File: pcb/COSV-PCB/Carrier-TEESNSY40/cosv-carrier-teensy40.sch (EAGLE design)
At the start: 25 parts, among them X1 057-006-1, X3 22-23-2031, X4 22-23-2031, X5 22-23-2031, X6 22-23-2031, X7 22-23-2031

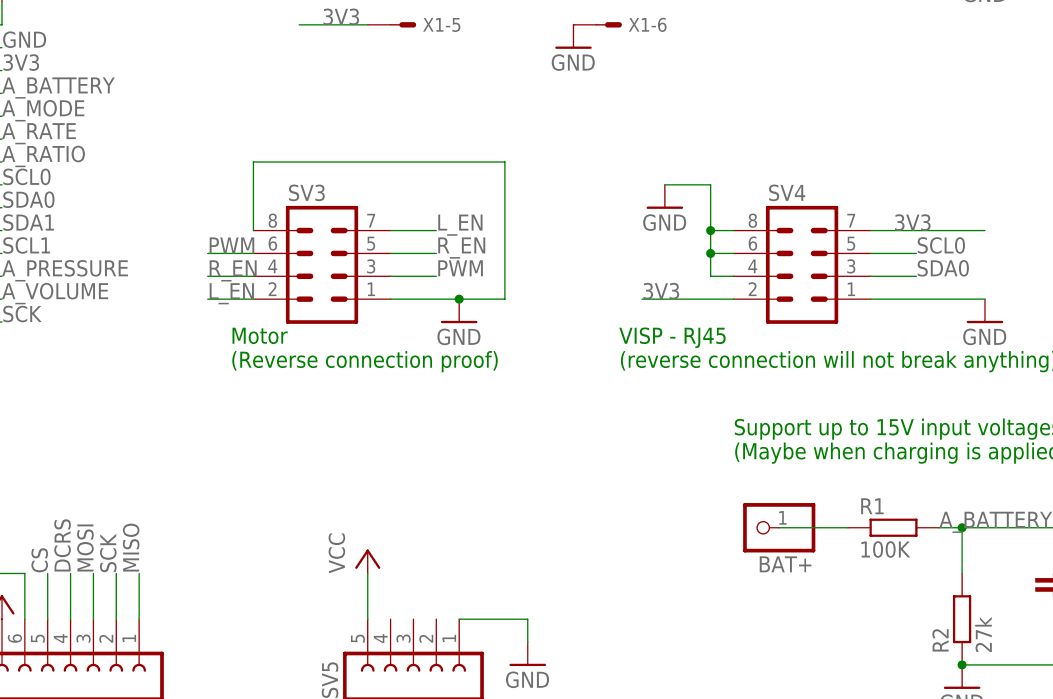
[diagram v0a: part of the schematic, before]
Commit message: Make the motor connector identical to the Arduino IBT_2 H-Bridge
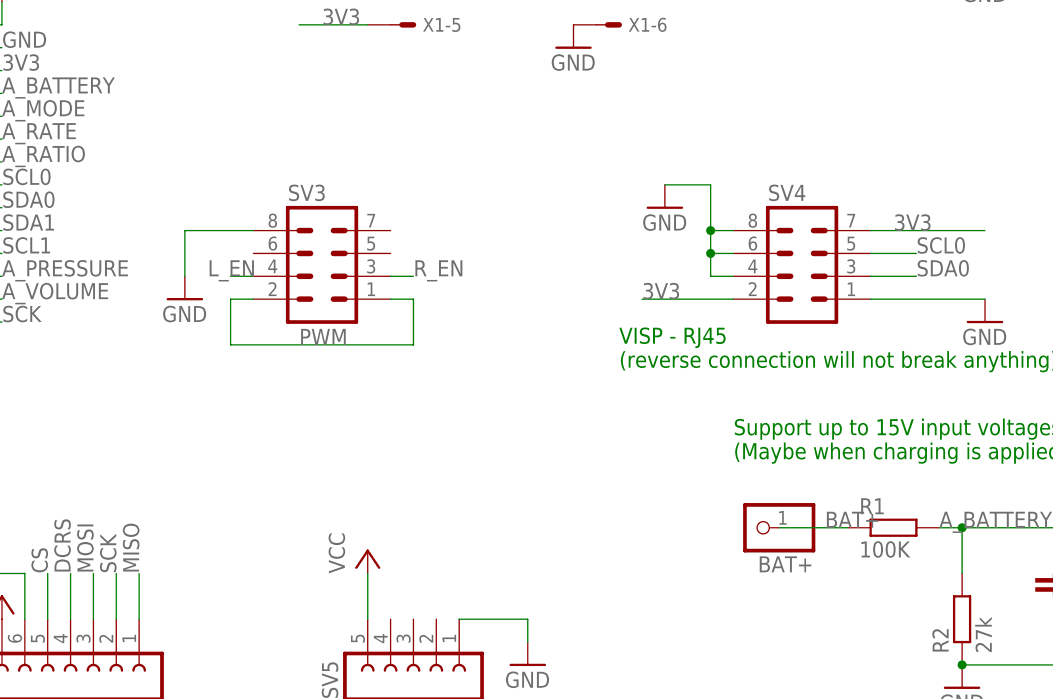
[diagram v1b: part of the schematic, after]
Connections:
- net N$2 renamed BAT+
- net GND: no longer SV3.1
- net L_EN: now also SV3.4; no longer SV3.2, SV3.7
- net PWM: now also SV3.1, SV3.2; no longer SV3.3, SV3.6
- net R_EN: now also SV3.3; no longer SV3.4, SV3.5
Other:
- note removed: "Motor (Reverse connection proof)"
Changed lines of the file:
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@@
 <?xml version="1.0" encoding="utf-8"?>
 <!DOCTYPE eagle SYSTEM "eagle.dtd">
-<eagle version="7.7.0">
+<eagle version="7.6.0">
 <drawing>
 <settings>
@@
 (Reverse connection swaps HOME/ENCODER)
 (Can be identified in software)</text>
-<text x="60.96" y="48.26" size="1.778" layer="91">Motor
-(Reverse connection proof)</text>
 <text x="104.14" y="48.26" size="1.778" layer="91">VISP - RJ45
 (reverse connection will not break anything)</text>
@@
 <instance part="GND5" gate="1" x="144.78" y="53.34"/>
 <instance part="GND9" gate="1" x="109.22" y="66.04"/>
-<instance part="GND10" gate="1" x="86.36" y="53.34"/>
+<instance part="GND10" gate="1" x="55.88" y="55.88"/>
 <instance part="GND11" gate="1" x="99.06" y="83.82"/>
 <instance part="GND12" gate="1" x="58.42" y="93.98"/>
@@
 </segment>
 <segment>
-<pinref part="SV3" gate="G$1" pin="1"/>
-<pinref part="GND10" gate="1" pin="GND"/>
-<wire x1="78.74" y1="55.88" x2="86.36" y2="55.88" width="0.1524" layer="91"/>
-<pinref part="SV3" gate="G$1" pin="8"/>
-<wire x1="63.5" y1="63.5" x2="63.5" y2="71.12" width="0.1524" layer="91"/>
-<wire x1="63.5" y1="71.12" x2="91.44" y2="71.12" width="0.1524" layer="91"/>
-<wire x1="91.44" y1="71.12" x2="91.44" y2="55.88" width="0.1524" layer="91"/>
-<wire x1="91.44" y1="55.88" x2="86.36" y2="55.88" width="0.1524" layer="91"/>
-<junction x="86.36" y="55.88"/>
-</segment>
-<segment>
 <pinref part="X1" gate="-6" pin="S"/>
 <pinref part="GND11" gate="1" pin="GND"/>
@@
 <pinref part="GND13" gate="1" pin="GND"/>
 <wire x1="27.94" y1="25.4" x2="27.94" y2="20.32" width="0.1524" layer="91"/>
+</segment>
+<segment>
+<pinref part="SV3" gate="G$1" pin="8"/>
+<pinref part="GND10" gate="1" pin="GND"/>
+<wire x1="63.5" y1="63.5" x2="55.88" y2="63.5" width="0.1524" layer="91"/>
+<wire x1="55.88" y1="63.5" x2="55.88" y2="58.42" width="0.1524" layer="91"/>
 </segment>
 </net>
@@
 </segment>
 <segment>
-<pinref part="SV3" gate="G$1" pin="5"/>
-<wire x1="78.74" y1="60.96" x2="83.82" y2="60.96" width="0.1524" layer="91"/>
-<label x="83.82" y="60.96" size="1.778" layer="95"/>
-</segment>
-<segment>
-<pinref part="SV3" gate="G$1" pin="4"/>
-<wire x1="63.5" y1="58.42" x2="58.42" y2="58.42" width="0.1524" layer="91"/>
-<label x="58.42" y="58.42" size="1.778" layer="95"/>
+<pinref part="SV3" gate="G$1" pin="3"/>
+<wire x1="78.74" y1="58.42" x2="81.28" y2="58.42" width="0.1524" layer="91"/>
+<label x="81.28" y="58.42" size="1.778" layer="95"/>
 </segment>
 </net>
@@
 </segment>
 <segment>
-<pinref part="SV3" gate="G$1" pin="7"/>
-<wire x1="78.74" y1="63.5" x2="83.82" y2="63.5" width="0.1524" layer="91"/>
-<label x="83.82" y="63.5" size="1.778" layer="95"/>
-</segment>
-<segment>
-<pinref part="SV3" gate="G$1" pin="2"/>
-<wire x1="63.5" y1="55.88" x2="58.42" y2="55.88" width="0.1524" layer="91"/>
-<label x="58.42" y="55.88" size="1.778" layer="95"/>
+<pinref part="SV3" gate="G$1" pin="4"/>
+<wire x1="63.5" y1="58.42" x2="60.96" y2="58.42" width="0.1524" layer="91"/>
+<label x="58.42" y="58.42" size="1.778" layer="95"/>
 </segment>
 </net>
@@
 </segment>
 <segment>
-<pinref part="SV3" gate="G$1" pin="3"/>
-<wire x1="78.74" y1="58.42" x2="83.82" y2="58.42" width="0.1524" layer="91"/>
-<label x="83.82" y="58.42" size="1.778" layer="95"/>
-</segment>
-<segment>
-<pinref part="SV3" gate="G$1" pin="6"/>
-<wire x1="63.5" y1="60.96" x2="58.42" y2="60.96" width="0.1524" layer="91"/>
-<label x="58.42" y="60.96" size="1.778" layer="95"/>
+<pinref part="SV3" gate="G$1" pin="2"/>
+<label x="68.58" y="50.8" size="1.778" layer="95"/>
+<wire x1="63.5" y1="55.88" x2="60.96" y2="55.88" width="0.1524" layer="91"/>
+<wire x1="60.96" y1="55.88" x2="60.96" y2="50.8" width="0.1524" layer="91"/>
+<pinref part="SV3" gate="G$1" pin="1"/>
+<wire x1="78.74" y1="55.88" x2="81.28" y2="55.88" width="0.1524" layer="91"/>
+<wire x1="60.96" y1="50.8" x2="81.28" y2="50.8" width="0.1524" layer="91"/>
+<wire x1="81.28" y1="50.8" x2="81.28" y2="55.88" width="0.1524" layer="91"/>
 </segment>
 </net>
@@
 </segment>
 </net>
-<net name="N$2" class="0">
+<net name="BAT+" class="0">
 <segment>
 <pinref part="BAT+" gate="A" pin="1"/>
 <pinref part="R1" gate="G$1" pin="1"/>
 <wire x1="121.92" y1="30.48" x2="129.54" y2="30.48" width="0.1524" layer="91"/>
-</segment>
-</net>
+<label x="127" y="30.48" size="1.778" layer="95"/>
+</segment>
+</net>

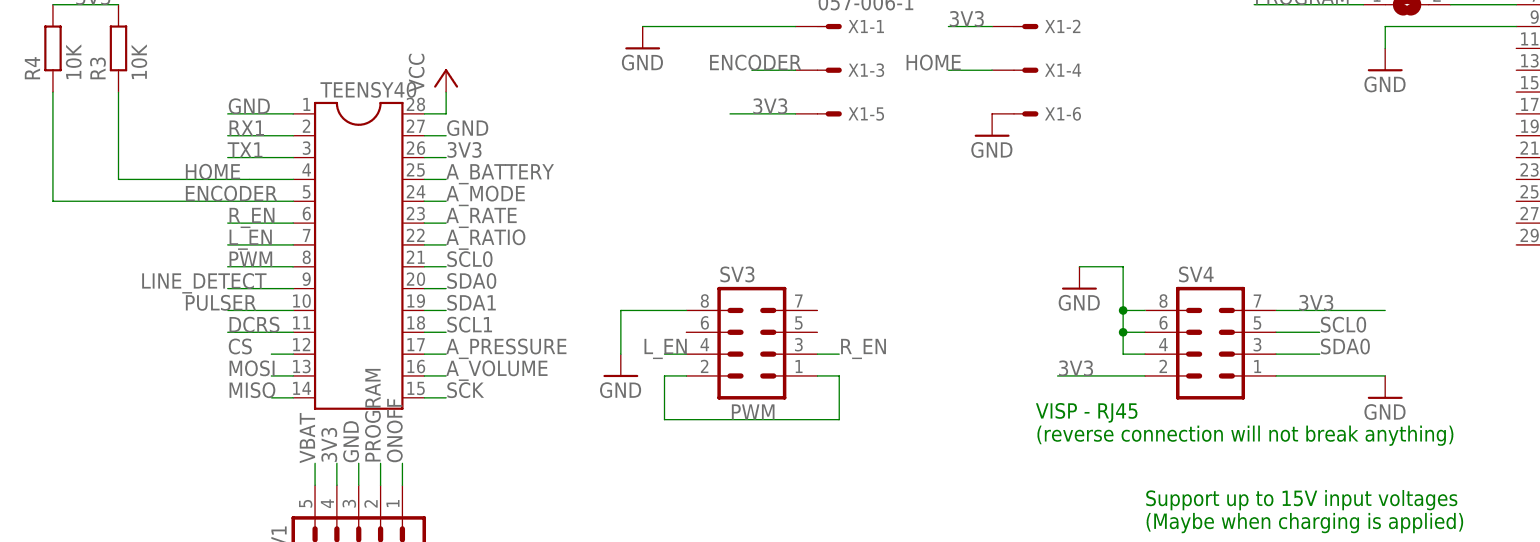
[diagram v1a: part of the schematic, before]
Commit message: Add second I2C channel to VISP connector
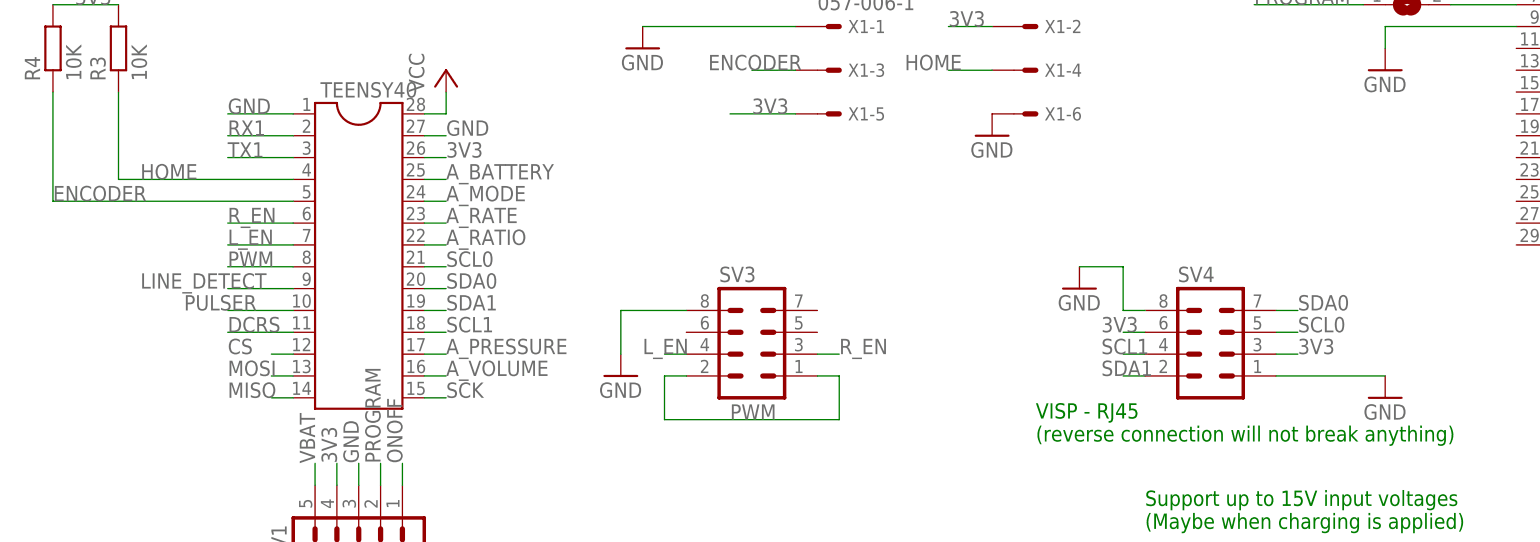
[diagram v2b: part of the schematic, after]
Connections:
- net 3V3: now also SV4.3, SV4.6; no longer SV4.2, SV4.7
- net GND: no longer SV4.4, SV4.6
- net SCL1: now also SV4.4
- net SDA0: now also SV4.7; no longer SV4.3
- net SDA1: now also SV4.2
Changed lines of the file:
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@@
 </segment>
 <segment>
-<pinref part="SV4" gate="G$1" pin="4"/>
-<wire x1="114.3" y1="58.42" x2="116.84" y2="58.42" width="0.1524" layer="91"/>
-<wire x1="114.3" y1="58.42" x2="114.3" y2="60.96" width="0.1524" layer="91"/>
-<pinref part="SV4" gate="G$1" pin="6"/>
-<wire x1="114.3" y1="60.96" x2="116.84" y2="60.96" width="0.1524" layer="91"/>
-<wire x1="114.3" y1="60.96" x2="114.3" y2="63.5" width="0.1524" layer="91"/>
 <pinref part="SV4" gate="G$1" pin="8"/>
 <wire x1="114.3" y1="63.5" x2="116.84" y2="63.5" width="0.1524" layer="91"/>
@@
 <pinref part="GND9" gate="1" pin="GND"/>
 <wire x1="114.3" y1="68.58" x2="109.22" y2="68.58" width="0.1524" layer="91"/>
-<junction x="114.3" y="60.96"/>
-<junction x="114.3" y="63.5"/>
 </segment>
 <segment>
@@
 </segment>
 <segment>
-<pinref part="SV4" gate="G$1" pin="3"/>
-<wire x1="132.08" y1="58.42" x2="137.16" y2="58.42" width="0.1524" layer="91"/>
-<label x="137.16" y="58.42" size="1.778" layer="95"/>
+<pinref part="SV4" gate="G$1" pin="7"/>
+<wire x1="132.08" y1="63.5" x2="134.62" y2="63.5" width="0.1524" layer="91"/>
+<label x="134.62" y="63.5" size="1.778" layer="95"/>
 </segment>
 </net>
@@
 <segment>
 <pinref part="SV4" gate="G$1" pin="5"/>
-<wire x1="132.08" y1="60.96" x2="137.16" y2="60.96" width="0.1524" layer="91"/>
-<label x="137.16" y="60.96" size="1.778" layer="95"/>
+<wire x1="132.08" y1="60.96" x2="134.62" y2="60.96" width="0.1524" layer="91"/>
+<label x="134.62" y="60.96" size="1.778" layer="95"/>
 </segment>
 </net>
@@
 <segment>
 <pinref part="TEENSY40" gate="G$1" pin="4"/>
-<wire x1="17.78" y1="78.74" x2="12.7" y2="78.74" width="0.1524" layer="91"/>
-<label x="5.08" y="78.74" size="1.778" layer="95"/>
+<label x="0" y="78.74" size="1.778" layer="95"/>
 <pinref part="R3" gate="G$1" pin="1"/>
-<wire x1="12.7" y1="78.74" x2="10.16" y2="78.74" width="0.1524" layer="91"/>
-<wire x1="10.16" y1="78.74" x2="-2.54" y2="78.74" width="0.1524" layer="91"/>
+<wire x1="17.78" y1="78.74" x2="-2.54" y2="78.74" width="0.1524" layer="91"/>
 <wire x1="-2.54" y1="78.74" x2="-2.54" y2="88.9" width="0.1524" layer="91"/>
 </segment>
@@
 <segment>
 <pinref part="TEENSY40" gate="G$1" pin="5"/>
-<label x="5.08" y="76.2" size="1.778" layer="95"/>
+<label x="-10.16" y="76.2" size="1.778" layer="95"/>
 <pinref part="R4" gate="G$1" pin="1"/>
 <wire x1="17.78" y1="76.2" x2="-10.16" y2="76.2" width="0.1524" layer="91"/>
@@
 </segment>
 <segment>
-<pinref part="SV4" gate="G$1" pin="2"/>
-<wire x1="116.84" y1="55.88" x2="106.68" y2="55.88" width="0.1524" layer="91"/>
-<label x="106.68" y="55.88" size="1.778" layer="95"/>
-</segment>
-<segment>
-<pinref part="SV4" gate="G$1" pin="7"/>
-<wire x1="132.08" y1="63.5" x2="144.78" y2="63.5" width="0.1524" layer="91"/>
-<label x="134.62" y="63.5" size="1.778" layer="95"/>
+<pinref part="SV4" gate="G$1" pin="3"/>
+<wire x1="132.08" y1="58.42" x2="134.62" y2="58.42" width="0.1524" layer="91"/>
+<label x="134.62" y="58.42" size="1.778" layer="95"/>
+</segment>
+<segment>
+<pinref part="SV4" gate="G$1" pin="6"/>
+<wire x1="116.84" y1="60.96" x2="114.3" y2="60.96" width="0.1524" layer="91"/>
+<label x="111.76" y="60.96" size="1.778" layer="95"/>
 </segment>
 </net>
@@
 <label x="35.56" y="63.5" size="1.778" layer="95"/>
 </segment>
+<segment>
+<pinref part="SV4" gate="G$1" pin="2"/>
+<wire x1="116.84" y1="55.88" x2="114.3" y2="55.88" width="0.1524" layer="91"/>
+<label x="111.76" y="55.88" size="1.778" layer="95"/>
+</segment>
 </net>
 <net name="SCL1" class="0">
@@
 <label x="35.56" y="60.96" size="1.778" layer="95"/>
 </segment>
-</net>
+<segment>
+<pinref part="SV4" gate="G$1" pin="4"/>
+<wire x1="116.84" y1="58.42" x2="114.3" y2="58.42" width="0.1524" layer="91"/>
+<label x="111.76" y="58.42" size="1.778" layer="95"/>
+</segment>
+</net>
